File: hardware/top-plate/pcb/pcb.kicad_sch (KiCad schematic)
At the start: 46 parts, among them J1 Conn_01x02, SW1 SS-12D10L5

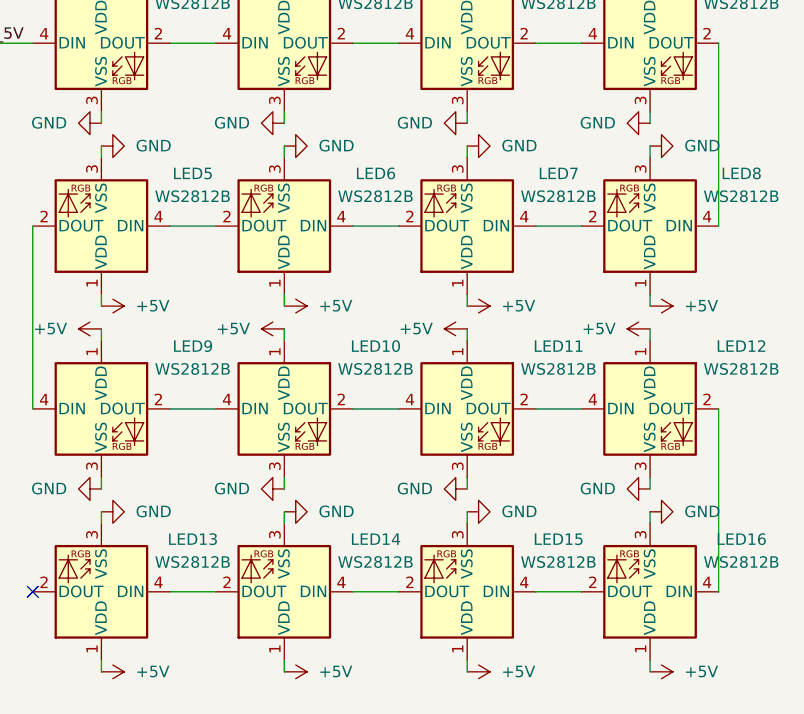
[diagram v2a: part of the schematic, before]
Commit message: added fuse to bottom plate
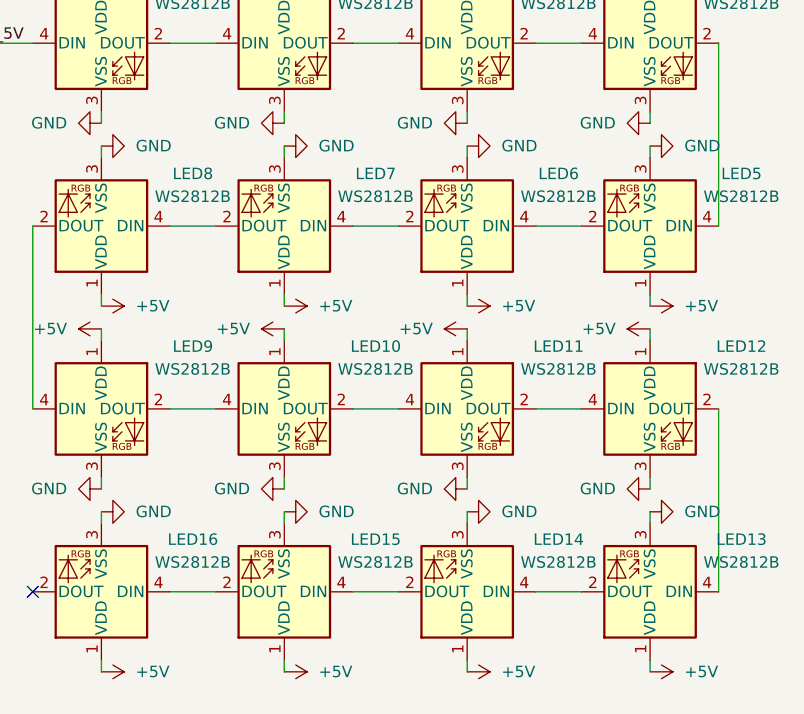
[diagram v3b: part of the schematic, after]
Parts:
- renumbered LED16 to LED13, LED15 to LED14, LED14 to LED15, LED13 to LED16, LED8 to LED5, LED7 to LED6, LED6 to LED7, LED5 to LED8
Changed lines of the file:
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@@
 		(dnp no)
 		(fields_autoplaced yes)
-		(property "Reference" "LED14"
+		(property "Reference" "LED15"
 			(at 350.52 102.1459 0)
 			(effects
@@
 			(project "top-plate"
 				(path "/2543a06c-fafe-4237-8cf7-5b57da9ea55c"
-					(reference "LED14")
+					(reference "LED15")
 					(unit 1)
 				)
@@
 		(dnp no)
 		(fields_autoplaced yes)
-		(property "Reference" "LED7"
+		(property "Reference" "LED6"
 			(at 370.84 61.5059 0)
 			(effects
@@
 			(project "top-plate"
 				(path "/2543a06c-fafe-4237-8cf7-5b57da9ea55c"
-					(reference "LED7")
+					(reference "LED6")
 					(unit 1)
 				)
@@
 		(dnp no)
 		(fields_autoplaced yes)
-		(property "Reference" "LED15"
+		(property "Reference" "LED14"
 			(at 370.84 102.1459 0)
 			(effects
@@
 			(project "top-plate"
 				(path "/2543a06c-fafe-4237-8cf7-5b57da9ea55c"
-					(reference "LED15")
+					(reference "LED14")
 					(unit 1)
 				)
@@
 		(dnp no)
 		(fields_autoplaced yes)
-		(property "Reference" "LED6"
+		(property "Reference" "LED7"
 			(at 350.52 61.5059 0)
 			(effects
@@
 			(project "top-plate"
 				(path "/2543a06c-fafe-4237-8cf7-5b57da9ea55c"
-					(reference "LED6")
+					(reference "LED7")
 					(unit 1)
 				)
@@
 		(dnp no)
 		(fields_autoplaced yes)
-		(property "Reference" "LED16"
+		(property "Reference" "LED13"
 			(at 391.16 102.1459 0)
 			(effects
@@
 			(project "top-plate"
 				(path "/2543a06c-fafe-4237-8cf7-5b57da9ea55c"
-					(reference "LED16")
+					(reference "LED13")
 					(unit 1)
 				)
@@
 		(dnp no)
 		(fields_autoplaced yes)
-		(property "Reference" "LED5"
+		(property "Reference" "LED8"
 			(at 330.2 61.5059 0)
 			(effects
@@
 			(project "top-plate"
 				(path "/2543a06c-fafe-4237-8cf7-5b57da9ea55c"
-					(reference "LED5")
+					(reference "LED8")
 					(unit 1)
 				)
@@
 		(dnp no)
 		(fields_autoplaced yes)
-		(property "Reference" "LED8"
+		(property "Reference" "LED5"
 			(at 391.16 61.5059 0)
 			(effects
@@
 			(project "top-plate"
 				(path "/2543a06c-fafe-4237-8cf7-5b57da9ea55c"
-					(reference "LED8")
+					(reference "LED5")
 					(unit 1)
 				)
@@
 		(dnp no)
 		(fields_autoplaced yes)
-		(property "Reference" "LED13"
+		(property "Reference" "LED16"
 			(at 330.2 102.1459 0)
 			(effects
@@
 			(project "top-plate"
 				(path "/2543a06c-fafe-4237-8cf7-5b57da9ea55c"
-					(reference "LED13")
+					(reference "LED16")
 					(unit 1)
 				)

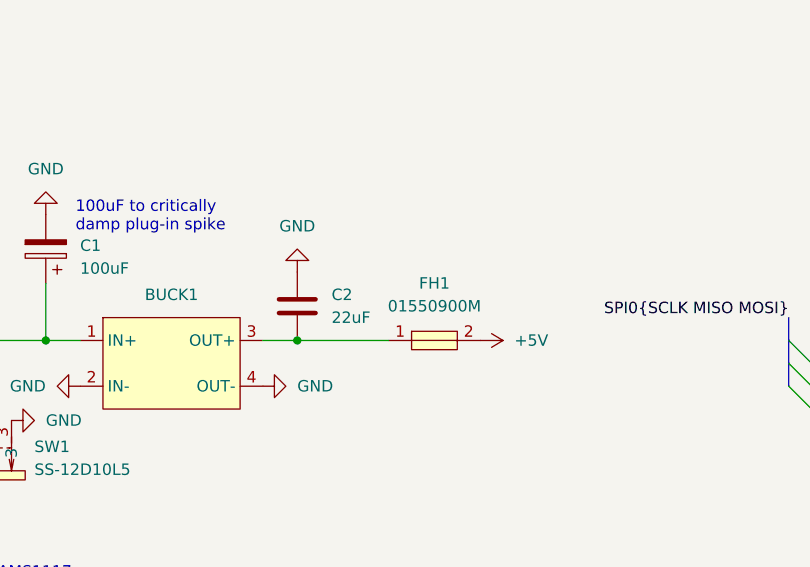
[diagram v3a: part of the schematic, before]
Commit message: added fuse to middle plate and fixed switches 3d view
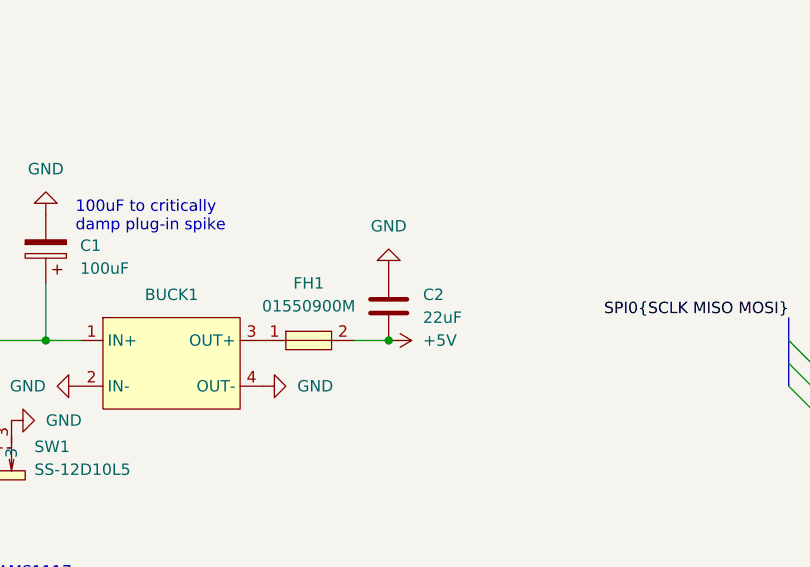
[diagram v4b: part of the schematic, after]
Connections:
- net +5V: now also C2.2
- net at BUCK1.3 (OUT+), FH1.1: no longer C2.2
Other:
- moved on the sheet: C2, FH1
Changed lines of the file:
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@@
 	)
 	(junction
-		(at 137.16 92.71)
+		(at 109.22 92.71)
 		(diameter 0)
 		(color 0 0 0 0)
 	)
 	(junction
-		(at 109.22 92.71)
+		(at 165.1 129.54)
 		(diameter 0)
 		(color 0 0 0 0)
 	)
 	(junction
-		(at 165.1 129.54)
+		(at 86.36 129.54)
 		(diameter 0)
 		(color 0 0 0 0)
 	)
 	(junction
-		(at 86.36 129.54)
+		(at 147.32 92.71)
 		(diameter 0)
 		(color 0 0 0 0)
@@
 	(wire
 		(pts
-			(xy 137.16 92.71) (xy 133.35 92.71)
-		)
-		(stroke
-			(width 0)
-			(type default)
-		)
-	)
-	(wire
-		(pts
 			(xy 209.55 250.19) (xy 223.52 250.19)
 		)
@@
 		)
 	)
-	(wire
-		(pts
-			(xy 137.16 92.71) (xy 147.32 92.71)
-		)
-		(stroke
-			(width 0)
-			(type default)
-		)
-	)
 	(bus
 		(pts
@@
 		)
 	)
+	(wire
+		(pts
+			(xy 143.51 92.71) (xy 147.32 92.71)
+		)
+		(stroke
+			(width 0)
+			(type default)
+		)
+	)
 	(bus
 		(pts
@@
 	(symbol
 		(lib_id "Device:C")
-		(at 137.16 88.9 0)
+		(at 147.32 88.9 0)
 		(mirror y)
 		(unit 1)
@@
 		(fields_autoplaced yes)
 		(property "Reference" "C2"
-			(at 140.97 87.6299 0)
+			(at 151.13 87.6299 0)
 			(effects
 				(font
@@
 		)
 		(property "Value" "22uF"
-			(at 140.97 90.1699 0)
+			(at 151.13 90.1699 0)
 			(effects
 				(font
@@
 		)
 		(property "Footprint" "PCM_Capacitor_SMD_AKL:C_0805_2012Metric_Pad1.15x1.40mm_HandSolder"
-			(at 136.1948 92.71 0)
+			(at 146.3548 92.71 0)
 			(effects
 				(font
@@
 		)
 		(property "Datasheet" "~"
-			(at 137.16 88.9 0)
+			(at 147.32 88.9 0)
 			(effects
 				(font
@@
 		)
 		(property "Description" "Unpolarized capacitor"
-			(at 137.16 88.9 0)
+			(at 147.32 88.9 0)
 			(effects
 				(font
@@
 	(symbol
 		(lib_id "power:+5V")
-		(at 157.48 92.71 270)
+		(at 147.32 92.71 270)
 		(mirror x)
 		(unit 1)
@@
 		(fields_autoplaced yes)
 		(property "Reference" "#PWR0107"
-			(at 153.67 92.71 0)
+			(at 143.51 92.71 0)
 			(effects
 				(font
@@
 		)
 		(property "Value" "+5V"
-			(at 161.29 92.7099 90)
+			(at 151.13 92.7099 90)
 			(effects
 				(font
@@
 		)
 		(property "Footprint" ""
-			(at 157.48 92.71 0)
+			(at 147.32 92.71 0)
 			(effects
 				(font
@@
 		)
 		(property "Datasheet" ""
-			(at 157.48 92.71 0)
+			(at 147.32 92.71 0)
 			(effects
 				(font
@@
 		)
 		(property "Description" "Power symbol creates a global label with name \"+5V\""
-			(at 157.48 92.71 0)
+			(at 147.32 92.71 0)
 			(effects
 				(font
@@
 	(symbol
 		(lib_id "EasyEDA:01550900M")
-		(at 152.4 92.71 0)
+		(at 138.43 92.71 0)
 		(unit 1)
 		(exclude_from_sim no)
@@
 		(fields_autoplaced yes)
 		(property "Reference" "FH1"
-			(at 152.4 86.36 0)
+			(at 138.43 86.36 0)
 			(effects
 				(font
@@
 		)
 		(property "Value" "01550900M"
-			(at 152.4 88.9 0)
+			(at 138.43 88.9 0)
 			(effects
 				(font
@@
 		)
 		(property "Footprint" "EasyEDA:FUSE-SMD_L9.8-W5.0"
-			(at 152.4 100.33 0)
+			(at 138.43 100.33 0)
 			(effects
 				(font
@@
 		)
 		(property "Datasheet" "https://lcsc.com/product-detail/Others_Littelfuse_01550900M_Littelfuse-01550900M_C108518.html"
-			(at 152.4 102.87 0)
+			(at 138.43 102.87 0)
 			(effects
 				(font
@@
 		)
 		(property "Description" ""
-			(at 152.4 92.71 0)
+			(at 138.43 92.71 0)
 			(effects
 				(font
@@
 		)
 		(property "LCSC Part" "C108518"
-			(at 152.4 105.41 0)
+			(at 138.43 105.41 0)
 			(effects
 				(font
@@
 	(symbol
 		(lib_id "power:GND")
-		(at 137.16 85.09 180)
+		(at 147.32 85.09 180)
 		(unit 1)
 		(exclude_from_sim no)
@@
 		(fields_autoplaced yes)
 		(property "Reference" "#PWR0106"
-			(at 137.16 78.74 0)
+			(at 147.32 78.74 0)
 			(effects
 				(font
@@
 		)
 		(property "Value" "GND"
-			(at 137.16 80.01 0)
+			(at 147.32 80.01 0)
 			(effects
 				(font
@@
 		)
 		(property "Footprint" ""
-			(at 137.16 85.09 0)
+			(at 147.32 85.09 0)
 			(effects
 				(font
@@
 		)
 		(property "Datasheet" ""
-			(at 137.16 85.09 0)
+			(at 147.32 85.09 0)
 			(effects
 				(font
@@
 		)
 		(property "Description" "Power symbol creates a global label with name \"GND\" , ground"
-			(at 137.16 85.09 0)
+			(at 147.32 85.09 0)
 			(effects
 				(font

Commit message: top pcb completed
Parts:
- added H10, H11, H12, H13, H14, H15, H16, H17, H18, H19, H20, H21, H22, H23, H24, H9: MountingHole_Pad, MountingHole:MountingHole_2.2mm_M2_Pad_Via, symbol Mechanical:MountingHole_Pad
- C1: footprint Capacitor_SMD:CP_Elec_5x5.7 -> Capacitor_SMD:CP_Elec_6.3x7.7
- MIC1: footprint INMP441:INMP441 -> INMP441:INMP441_SMD
- PWR1: value XT30-M -> Conn_01x02; footprint Connector_AMASS:AMASS_XT30U-M_1x02_P5.0mm_Vertical -> Connector_JST:JST_XH_B2B-XH-A_1x02_P2.50mm_Vertical
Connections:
- net I2C1.SCL is gone; now on net I2C0.SCL: R5.2
- net I2C1.SDA is gone; now on net I2C0.SDA: R4.2
- net DMUX1_INTA: now also MCU1.4 (GPIO2); no longer MCU1.34 (GPIO28_ADC2)
- net DMUX1_NRST: now also MCU1.11 (GPIO8); no longer MCU1.1 (GPIO0)
- net DMUX2_INTA: now also MCU1.31 (GPIO26_ADC0)
- net DMUX2_NRST: now also MCU1.29 (GPIO22); no longer MCU1.2 (GPIO1)
- net EN: now also J1.2 (Pin_2); no longer J1.1 (Pin_1)
- net IMU2.INT: now also MCU1.32 (GPIO27_ADC1)
- net IMU2.NCS: now also MCU1.34 (GPIO28_ADC2)
- net LED_SIG_3V3: now also MCU1.2 (GPIO1)
- net LED_SIG_DIR: now also MCU1.1 (GPIO0)
- net RUN: now also J1.1 (Pin_1); no longer J1.2 (Pin_2)
- net US_NRST: now also MCU1.5 (GPIO3)
- net I2C0.SDA: now reaches MCU1.26 (GPIO20)
- net I2C0.SCL: now reaches MCU1.27 (GPIO21)
- no-connect marks 22 -> 36
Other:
- sheet CH201 ports: added none; removed DMUX1_INTB, DMUX2_INTB
- note added: "Power from middle plate. Uses JST-XH for space and height. 3A@12V is plenty. Does not take 5V from bottom due to power concerns (there would not be enough to sustain absolutely everything running at peak)"
- note removed: "Power from middle plate. An JST-XH would be perfectly fine, but this signals clearly that it is power and enables easily plugging into LiPo directly. Does not take 5V from bottom due to power concerns (there would not be enough to sustain absolutely everything running at peak)"

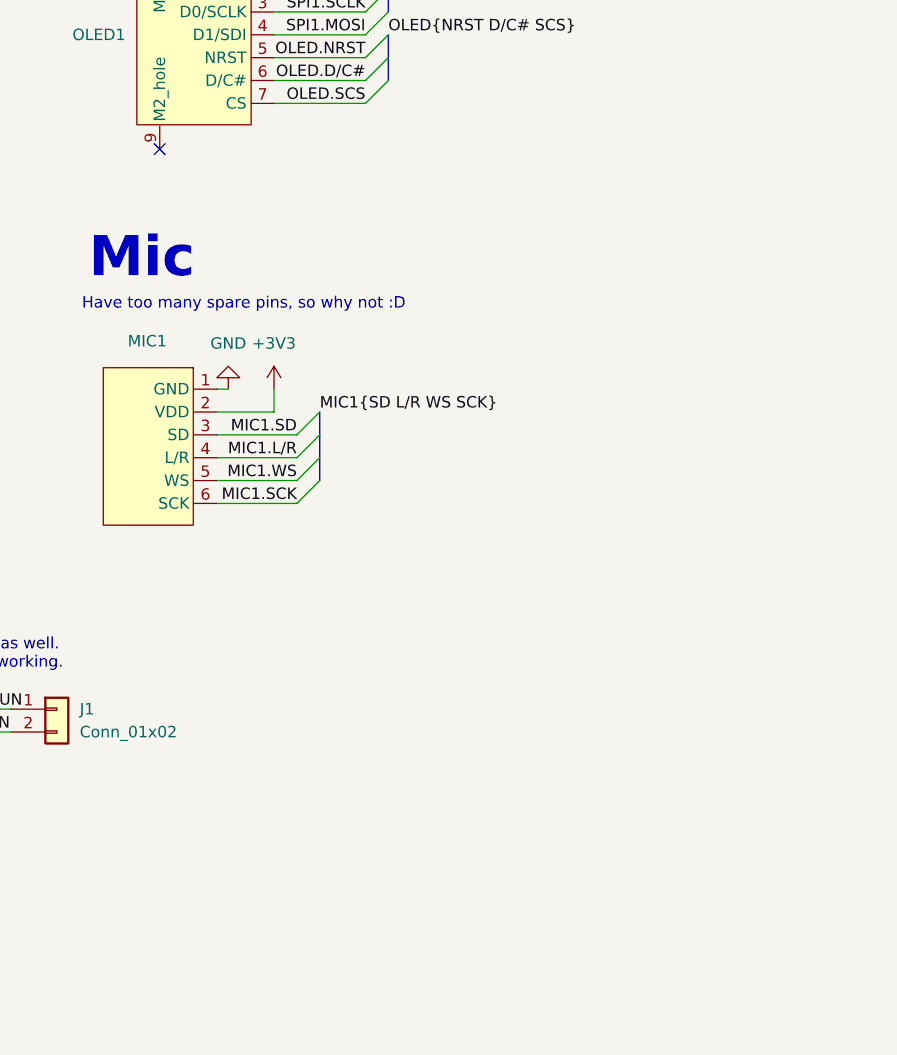
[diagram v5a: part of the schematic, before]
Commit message: labelled bottom middle and top pcbs, added testpoints
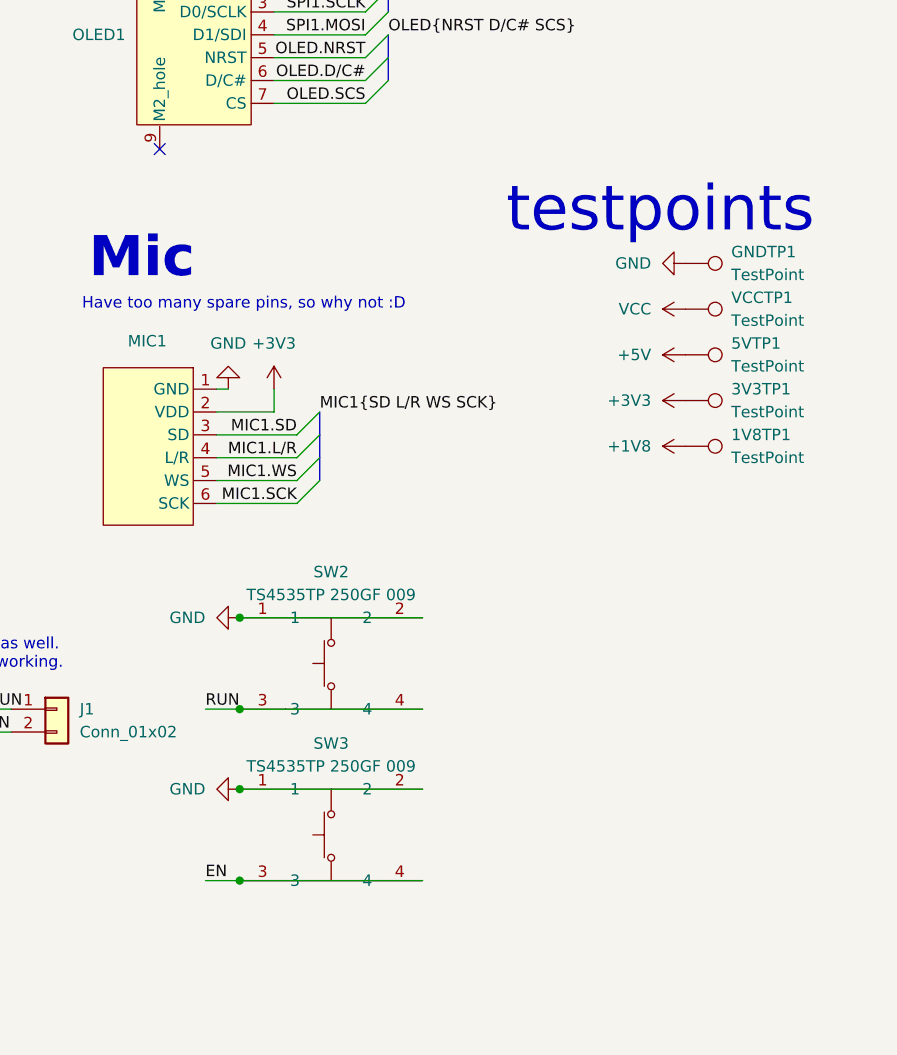
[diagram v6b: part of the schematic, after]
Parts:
- added 1V8TP1, 3V3TP1, 5VTP1, GNDTP1, VCCTP1: TestPoint, TestPoint:TestPoint_THTPad_D1.0mm_Drill0.5mm, symbol Connector:TestPoint
- added SW2, SW3: TS4535TP 250GF 009, EasyEDA:SW-SMD_4P-L4.5-W4.5-P3.00-LS6.8, symbol EasyEDA:TS4535TP250GF009
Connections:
- net +1V8: now also 1V8TP1.1
- net +3V3: now also 3V3TP1.1
- net +5V: now also 5VTP1.1
- net EN: now also SW3.3, SW3.4
- net GND: now also GNDTP1.1, SW2.1, SW2.2, SW3.1, SW3.2
- net RUN: now also SW2.3, SW2.4
- net VCC: now also VCCTP1.1
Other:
- note added: "testpoints"

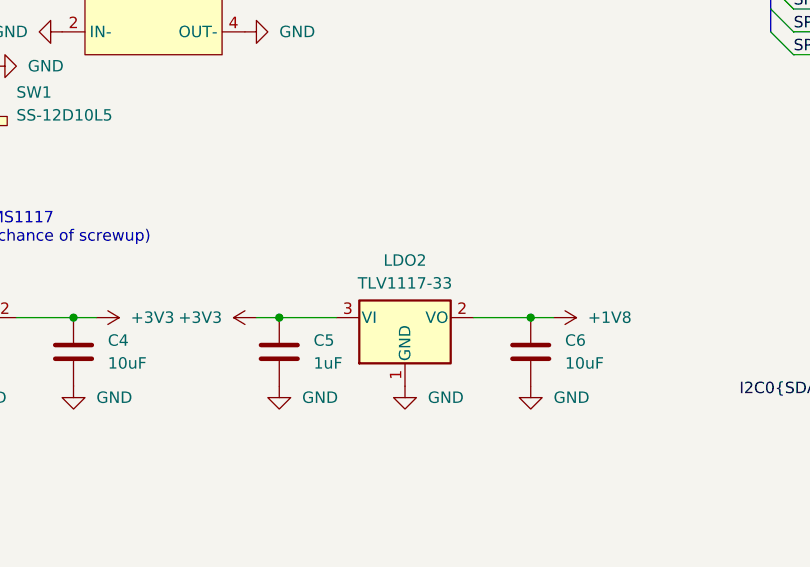
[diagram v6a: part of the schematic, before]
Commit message: changed tlv1117-33 to tlv1117-18 on top pcb for 1.8V LDO
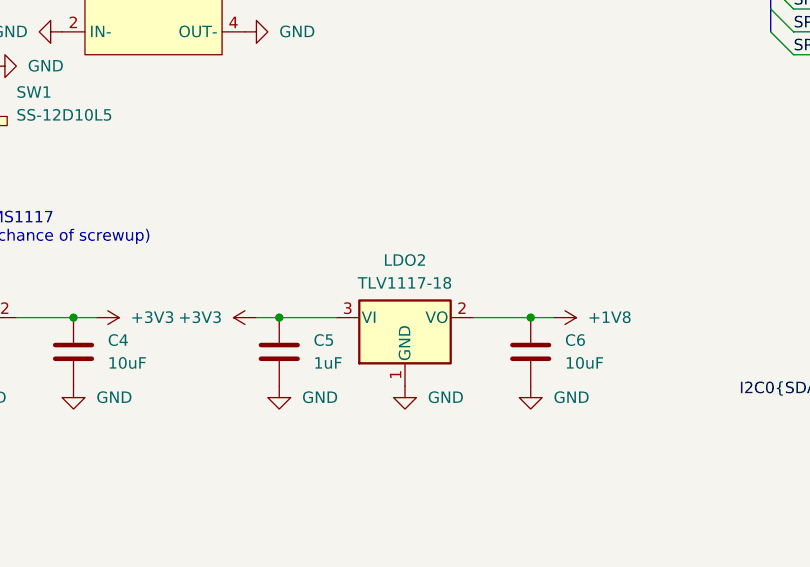
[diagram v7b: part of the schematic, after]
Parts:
- LDO2: value TLV1117-33 -> TLV1117-18
